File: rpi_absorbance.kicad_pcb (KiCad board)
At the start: 2 copper layers, 35 parts, among them CON1 BARREL_JACK, P1 CONN_02X04, P2 CONN_01X02, P3 RPI_HEADER, P4 STEPPER_CONN, P5 CONN_02X04, Q1 ZTX692B, U1 R-78B5.0-1.5L, U2 MUN5216DW1T1G, U3 DRV8825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

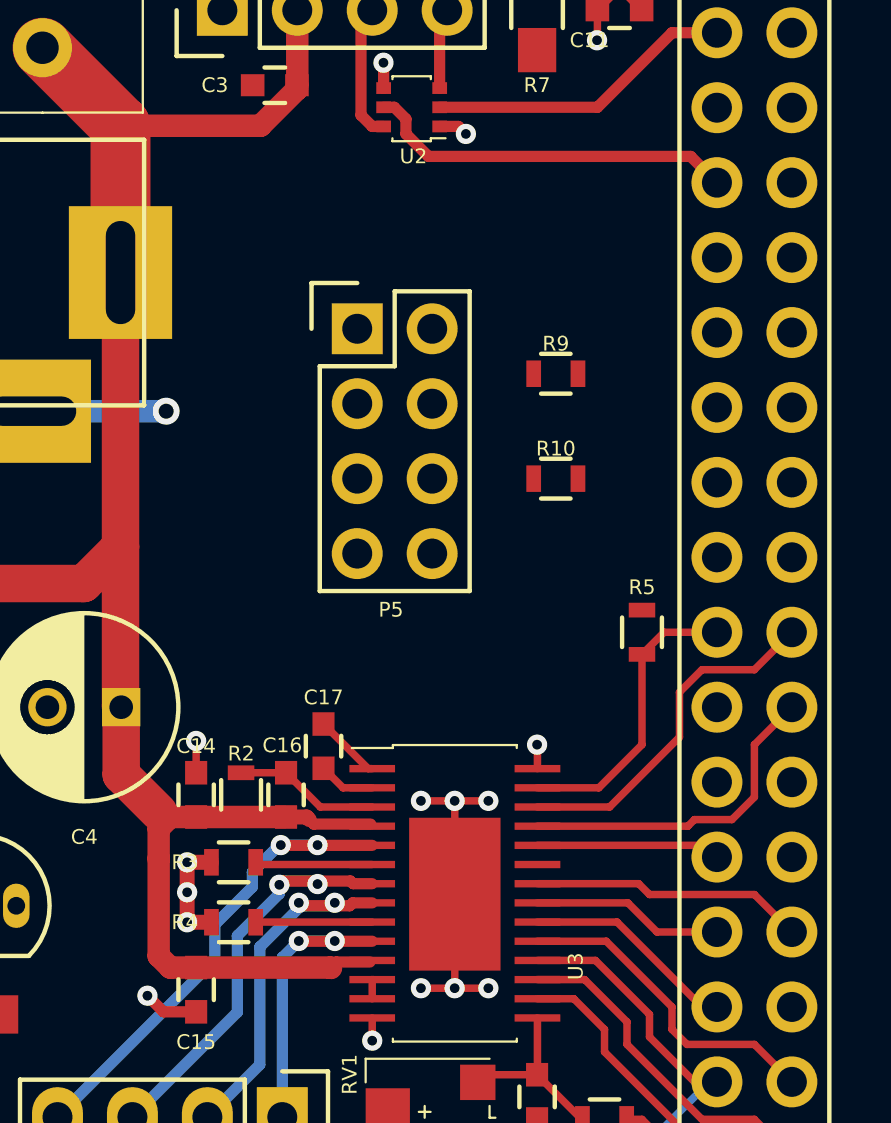
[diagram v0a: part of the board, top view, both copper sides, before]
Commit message: Start connecting gpio header
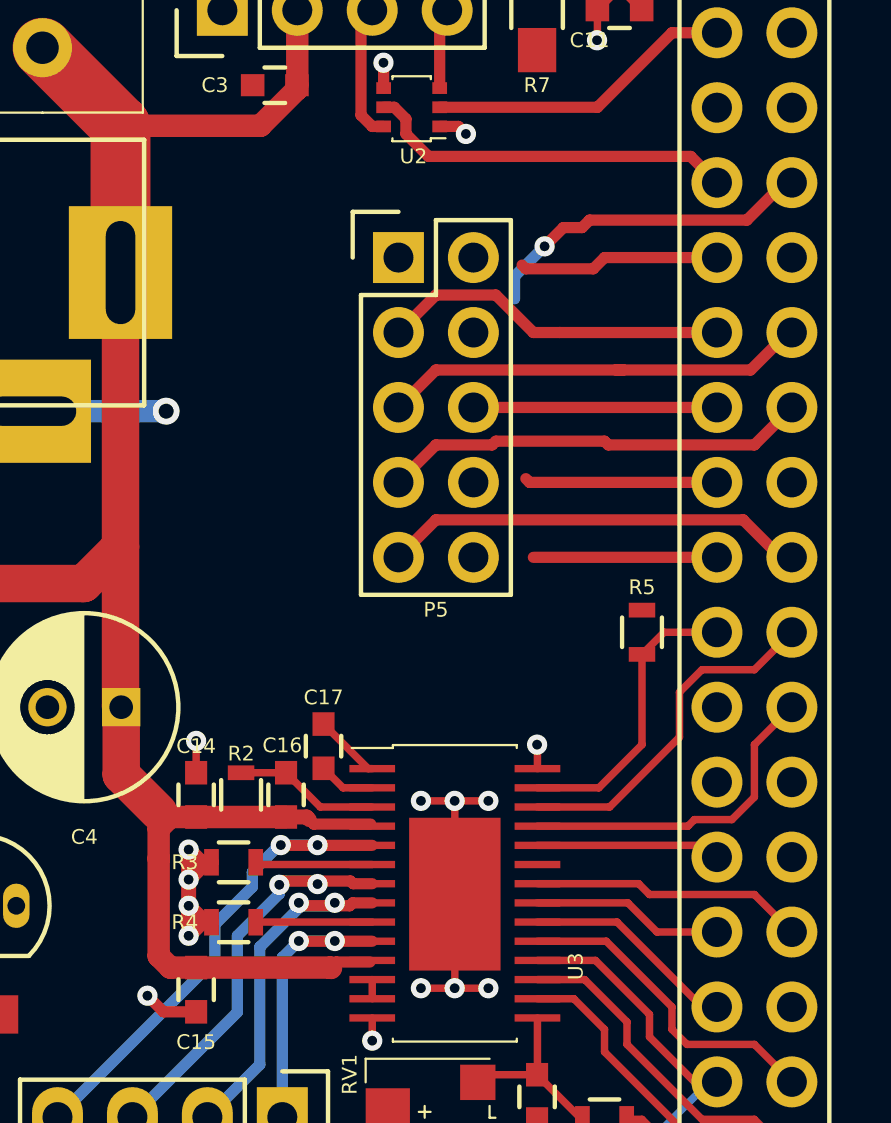
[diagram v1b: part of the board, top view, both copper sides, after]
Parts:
- removed R10, R9: 10k, Resistors_SMD:R_0603
- P5: value CONN_02X04 -> CONN_02X05; footprint Pin_Headers:Pin_Header_Straight_2x04 -> Pin_Headers:Pin_Header_Straight_2x05
- moved P5 2.79 mm to (168.8, 110.2)
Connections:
- P3 pad 12: (no net) -> /GPIO18
- P3 pad 13: /SWITCH1 -> /GPIO27
- P3 pad 15: /SWITCH2 -> /GPIO22
- P3 pad 16: (no net) -> /GPIO23
- P3 pad 18: (no net) -> /GPIO24
- P3 pad 22: (no net) -> /GPIO25
- P5 pad 2: GND -> /GPIO9
- P5 pad 3: /SWITCH1 -> /GPIO22
- P5 pad 5: /SWITCH2 -> /GPIO23
- P5 pad 6: /GPIO9 -> +3V3
- P5 pad 7: +3V3 -> /GPIO24
- P5 pad 8: (no net) -> /GPIO18
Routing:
- net /GPIO23: track 0.00 -> 14.6 mm
- net /GPIO24: track 0.00 -> 14.5 mm
- net /GPIO25: track 0.00 -> 14.4 mm
- net /GPIO22: track 0.00 -> 11.8 mm
- net /GPIO18: track 0.00 -> 11.5 mm, vias 0 -> 1
- net +3V3: track 9.08 -> 17.3 mm
- net /GPIO27: track 0.00 -> 6.81 mm
- net /GPIO10: track 0.00 -> 6.53 mm
- net /GPIO9: track 0.00 -> 6.22 mm
- net GND: track 33.8 -> 37.0 mm, vias 21 -> 22

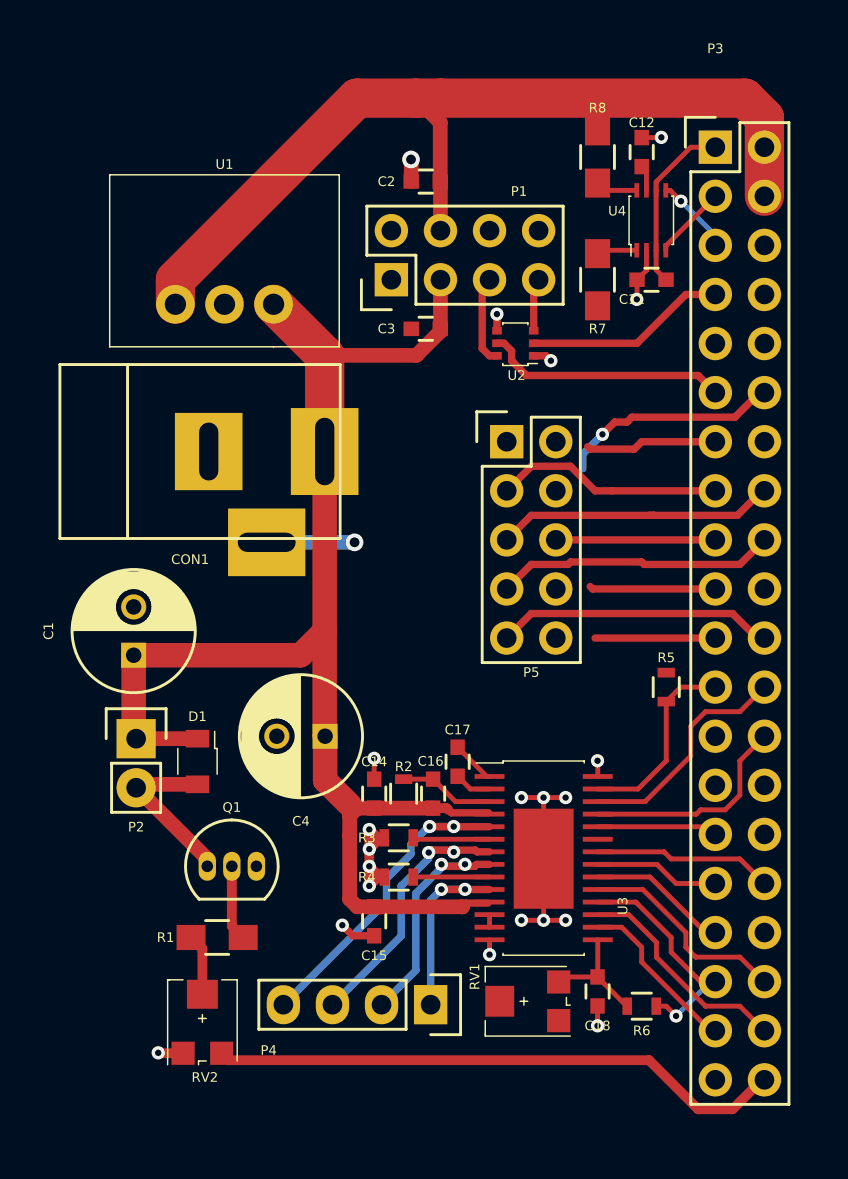
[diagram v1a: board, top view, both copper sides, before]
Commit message: Add labels and outline
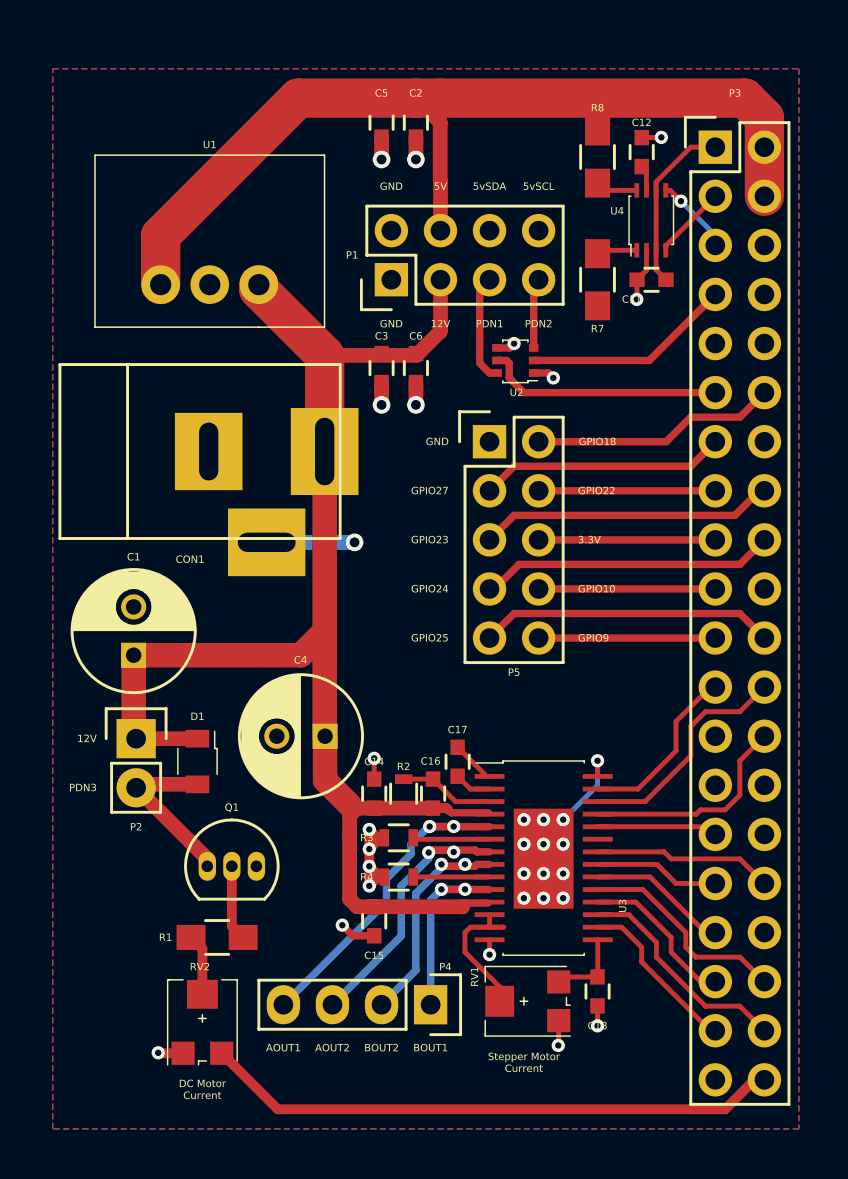
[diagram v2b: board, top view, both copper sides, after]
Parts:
- removed R5, R6: 10k, Resistors_SMD:R_0603
- added C5: .1u, Capacitors_SMD:C_0603, F.Cu at (162.3, 93.7)
- added C6: 10u, Capacitors_SMD:C_0603, F.Cu at (164.1, 106.4)
- C3: value 10u -> .1u
- moved C2 3.09 mm to (164.1, 93.7), turned to 270 degrees
- moved C3 3.06 mm to (162.3, 106.4), turned to 90 degrees
- moved U1 1.27 mm to (156.0, 102.1)
- moved U2 0.89 mm to (170.2, 106.7)
- moved P5 0.89 mm to (167.9, 110.2)
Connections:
- P5 pad 10: /GPIO27 -> /GPIO9
- P5 pad 2: /GPIO9 -> /GPIO18
- P5 pad 3: /GPIO22 -> /GPIO27
- P5 pad 4: /GPIO10 -> /GPIO22
- P5 pad 8: /GPIO18 -> /GPIO10
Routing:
- net GND: track 37.0 -> 71.3 mm, vias 22 -> 32
- net Net-(RV1-Pad2): track 0.65 -> 7.07 mm
- net /GPIO27: track 6.81 -> 12.7 mm
- net /nFAULT: track 12.2 -> 8.49 mm, vias 1 -> 0
- net /GPIO9: track 6.22 -> 9.14 mm
- net /GPIO22: track 11.8 -> 9.14 mm
- net /GPIO10: track 6.53 -> 9.14 mm
- net /V3P3: track 6.21 -> 4.05 mm
- net +12V: track 74.1 -> 75.4 mm
- net /GPIO18: track 11.5 -> 12.7 mm, vias 1 -> 0
- net +5V: track 48.8 -> 49.9 mm
- net Net-(P1-Pad5): track 4.64 -> 5.63 mm
- net /nHOME: track 10.1 -> 9.16 mm
- net +3V3: track 17.3 -> 18.2 mm
- net Net-(P1-Pad7): track 2.74 -> 3.63 mm
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- added copper zone on B.Cu, net GND
- added copper zone on F.Cu, net GND
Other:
- board text added: "12V"
- board text added: "3.3V"
- board text added: "5V"
- board text added: "5vSCL"
- board text added: "5vSDA"
- board text added: "AOUT1"
- board text added: "AOUT2"
- board text added: "BOUT1"
- board text added: "BOUT2"
- board text added: "DC Motor Current"
- board text added: "GND"
- board text added: "GPIO10"
- board text added: "GPIO18"
- board text added: "GPIO22"
- board text added: "GPIO23"
- board text added: "GPIO24"
- board text added: "GPIO25"
- board text added: "GPIO27"
- board text added: "GPIO9"
- board text added: "PDN1"
- board text added: "PDN2"
- board text added: "PDN3"
- board text added: "Stepper Motor Current"
